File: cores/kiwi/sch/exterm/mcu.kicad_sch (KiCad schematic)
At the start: 5 parts

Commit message: Schematics PDF moved to JTBIN
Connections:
- net ~{RST} renamed ~{MCU_RST}
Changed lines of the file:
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@@
     (stroke (width 0) (type default) (color 0 0 0 0))
   )
-  (wire (pts (xy 33.02 76.2) (xy 43.18 76.2))
+  (wire (pts (xy 35.56 76.2) (xy 43.18 76.2))
     (stroke (width 0) (type default) (color 0 0 0 0))
   )
@@
     (effects (font (size 1.27 1.27)) (justify right))
   )
-  (hierarchical_label "~{RST}" (shape input) (at 33.02 76.2 180)
-    (effects (font (size 1.27 1.27)) (justify right))
-  )
+  (hierarchical_label "~{MCU_RST}" (shape input) (at 35.56 76.2 180)
+    (effects (font (size 1.27 1.27)) (justify right))
+  )

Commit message: issue#46
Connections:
- net H1B renamed H1_BUF
- net ~{H1B} renamed ~{H1_BUF}
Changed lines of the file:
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@@
     (effects (font (size 1.27 1.27)) (justify right bottom))
   )
-  (label "H1B" (at 24.13 125.73 0)
+  (label "H1_BUF" (at 24.13 125.73 0)
     (effects (font (size 1.27 1.27)) (justify left bottom))
   )
@@
     (effects (font (size 1.27 1.27)) (justify left bottom))
   )
-  (label "~{H1B}" (at 29.21 73.66 0)
+  (label "~{H1_BUF}" (at 29.21 73.66 0)
     (effects (font (size 1.27 1.27)) (justify left bottom))
   )
@@
     (effects (font (size 1.27 1.27)) (justify left bottom))
   )
-  (label "~{H1B}" (at 71.12 125.73 180)
+  (label "~{H1_BUF}" (at 71.12 125.73 180)
     (effects (font (size 1.27 1.27)) (justify right bottom))
   )
@@
     (effects (font (size 1.27 1.27)) (justify right))
   )
-  (hierarchical_label "H1B" (shape input) (at 34.29 71.12 180)
+  (hierarchical_label "H1_BUF" (shape input) (at 34.29 71.12 180)
     (effects (font (size 1.27 1.27)) (justify right))
   )

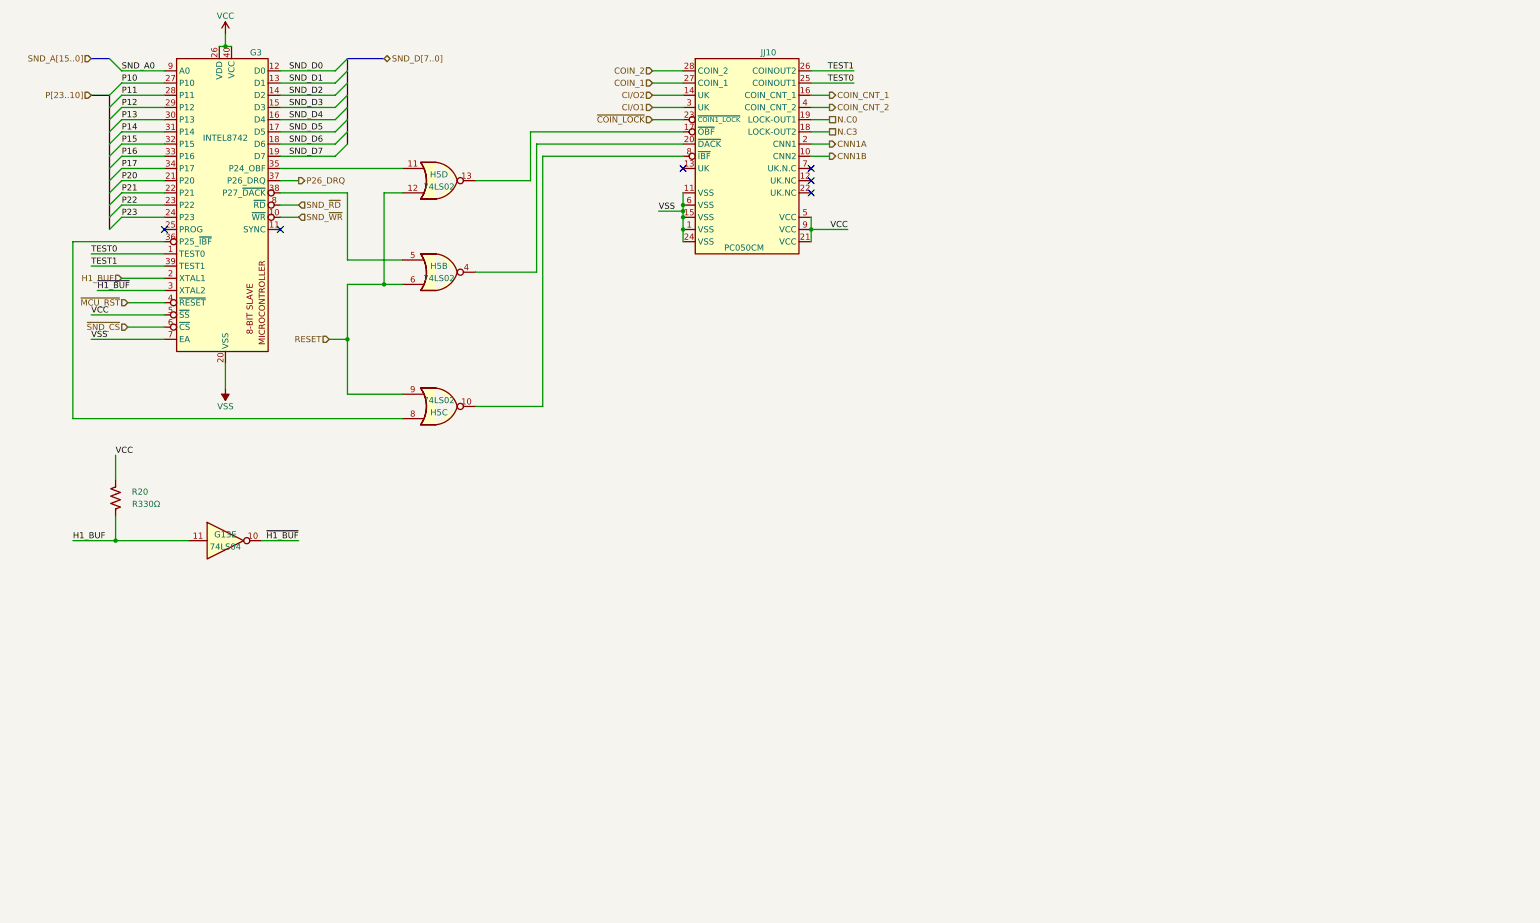
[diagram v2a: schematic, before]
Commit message: sheet_size_update
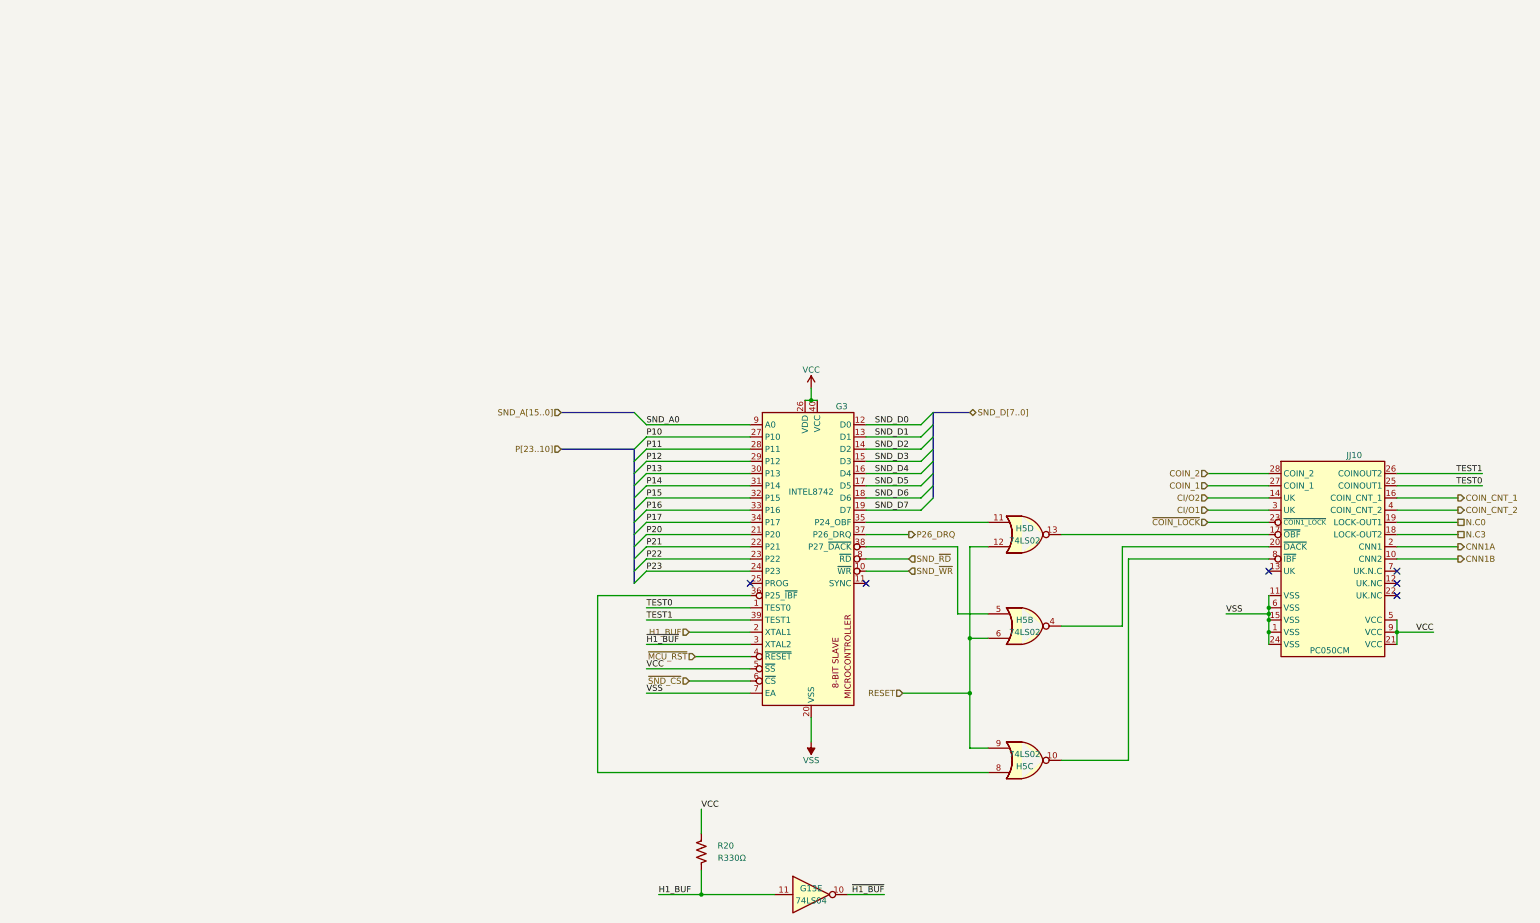
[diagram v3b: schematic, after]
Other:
- moved on the sheet: G13E, G3, H5B, H5C, H5D, JJ10, R20
